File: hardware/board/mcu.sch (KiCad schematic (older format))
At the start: 23 parts, among them J2 SWD, J3 USB_B_Receptacle, SW2 Reset, U5 ATSAMD51J20A-M, Y1 32.768 kHz

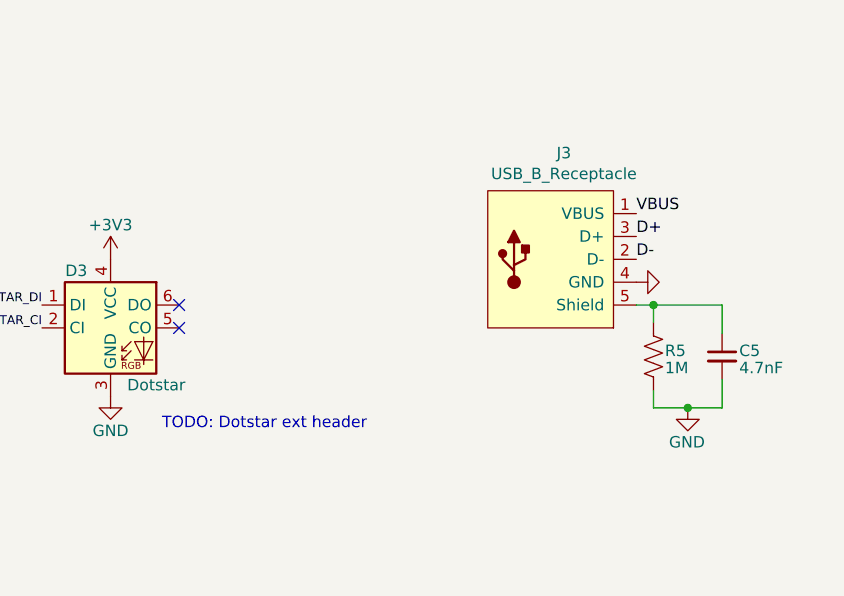
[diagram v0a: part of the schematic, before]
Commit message: More updates to the board design
- Added polyfuses for downstream power
- Added breakout header for external, panel-mounted USB port
- Added I/O breakout for the switches and buttons on the front control panel
- Made the MCU footprint a hybrid QFP/QFN footprint
- Add a nice illustration to the board backside
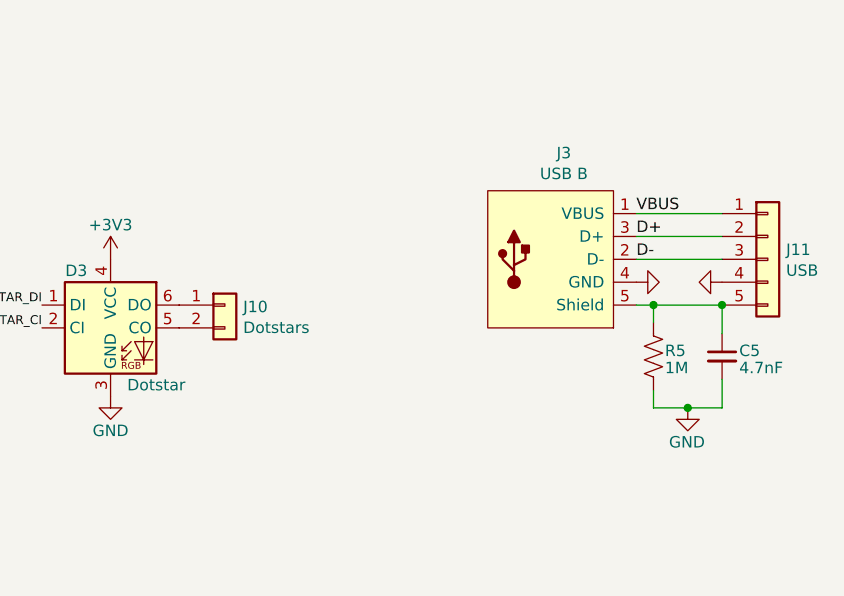
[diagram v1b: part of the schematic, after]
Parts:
- added J10: Dotstars, Connector_PinHeader_2.54mm:PinHeader_1x02_P2.54mm_Vertical, symbol Connector_Generic:Conn_01x02
- added J11: USB, Connector_PinHeader_2.54mm:PinHeader_1x05_P2.54mm_Vertical, symbol Connector_Generic:Conn_01x05
- J3: value USB_B_Receptacle -> USB B
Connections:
- net D+: now also J11.2 (Pin_2)
- net D-: now also J11.3 (Pin_3)
- net GND: now also J11.4 (Pin_4)
- net VBUS: now also J11.1 (Pin_1)
- net at D3.5 (CO): now also J10.2 (Pin_2)
- net at D3.6 (DO): now also J10.1 (Pin_1)
- net at C5.1, J3.5 (Shield), R5.1: now also J11.5 (Pin_5)
- no-connect marks 5 -> 3
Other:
- note removed: "TODO: Dotstar ext header"
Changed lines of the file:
@@
 Sheet 3 7
 Title "Hubble Motherboard"
-Date "2021-11-12"
+Date "2021-11-20"
 Rev "v2"
 Comp "Winterbloom"
 Comment1 "Alethea Flowers"
 Comment2 "CERN-OHL-P V2"
-Comment3 ""
+Comment3 "hubble.wntr.dev"
 Comment4 ""
 $EndDescr
@@
 	1    0    0    -1
 $EndComp
-NoConn ~ 8400 5925
-NoConn ~ 8400 5825
 Text Label 10475 1725 0    39   ~ 0
 DOTSTAR_CI
@@
 P 10050 5625
 F 0 "J3" H 10083 6090 50  0000 C CNN
-F 1 "USB_B_Receptacle" H 10083 5999 50  0000 C CNN
+F 1 "USB B" H 10083 5999 50  0000 C CNN
 F 2 "Connector_USB:USB_B_OST_USB-B1HSxx_Horizontal" H 10250 5575 50  0001 C CNN
 F 3 "https://www.te.com/commerce/DocumentDelivery/DDEController?Action=srchrtrv&DocNm=5787834&DocType=Customer+Drawing&DocLang=English&PartCntxt=5787834-1&DocFormat=pdf" H 10250 5575 50  0001 C CNN
@@
 Text HLabel 3575 1250 1    50   Input ~ 0
 PB22
-Text Notes 8325 6375 0    50   ~ 0
-TODO: Dotstar ext header
 Text HLabel 2175 1250 1    50   Input ~ 0
 PB02
@@
 Text HLabel 3375 1250 1    50   Input ~ 0
 PA27
+$Comp
+L Connector_Generic:Conn_01x05 J11
+U 1 1 6198BFAF
+P 10975 5625
+F 0 "J11" H 11055 5667 50  0000 L CNN
+F 1 "USB" H 11055 5576 50  0000 L CNN
+F 2 "Connector_PinHeader_2.54mm:PinHeader_1x05_P2.54mm_Vertical" H 10975 5625 50  0001 C CNN
+F 3 "~" H 10975 5625 50  0001 C CNN
+	1    10975 5625
+	1    0    0    -1
+$EndComp
+Connection ~ 10775 5825
+Wire Wire Line
+	10400 5425 10775 5425
+Wire Wire Line
+	10400 5525 10775 5525
+Wire Wire Line
+	10775 5625 10400 5625
+$Comp
+L power:GND #PWR?
+U 1 1 6199095B
+P 10775 5725
+AR Path="/6091A4E3/6199095B" Ref="#PWR?"  Part="1"
+AR Path="/608B4064/6199095B" Ref="#PWR0219"  Part="1"
+F 0 "#PWR0219" H 10775 5475 50  0001 C CNN
+F 1 "GND" H 10780 5552 50  0001 C CNN
+F 2 "" H 10775 5725 50  0001 C CNN
+F 3 "" H 10775 5725 50  0001 C CNN
+	1    10775 5725
+	0    1    1    0
+$EndComp
+$Comp
+L Connector_Generic:Conn_01x02 J10
+U 1 1 6199B10E
+P 8600 5825
+F 0 "J10" H 8680 5817 50  0000 L CNN
+F 1 "Dotstars" H 8680 5726 50  0000 L CNN
+F 2 "Connector_PinHeader_2.54mm:PinHeader_1x02_P2.54mm_Vertical" H 8600 5825 50  0001 C CNN
+F 3 "~" H 8600 5825 50  0001 C CNN
+	1    8600 5825
+	1    0    0    -1
+$EndComp
 $EndSCHEMATC
